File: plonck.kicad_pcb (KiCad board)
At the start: 2 copper layers, 228.6 x 76.2 mm, 127 parts, among them J1 Battery_connector, J2 SWD, Q1 Q_PMOS_DSG, U1 SRV05-4, U2 MCP73831-2-OT, U3 XC6206PxxxMR-Regulator_Linear, U4 nRF52840_holyiot_18010, q1 USB4085-GF-A_REVA

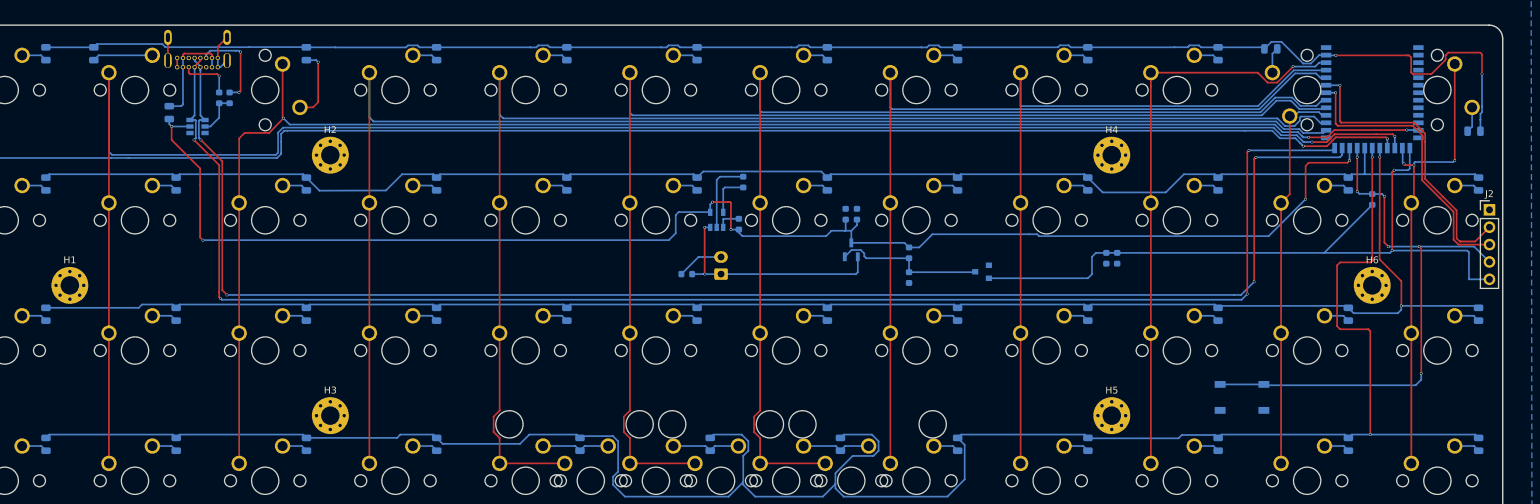
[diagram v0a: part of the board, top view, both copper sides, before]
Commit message: updated some fooprints and added lcsc part numbers
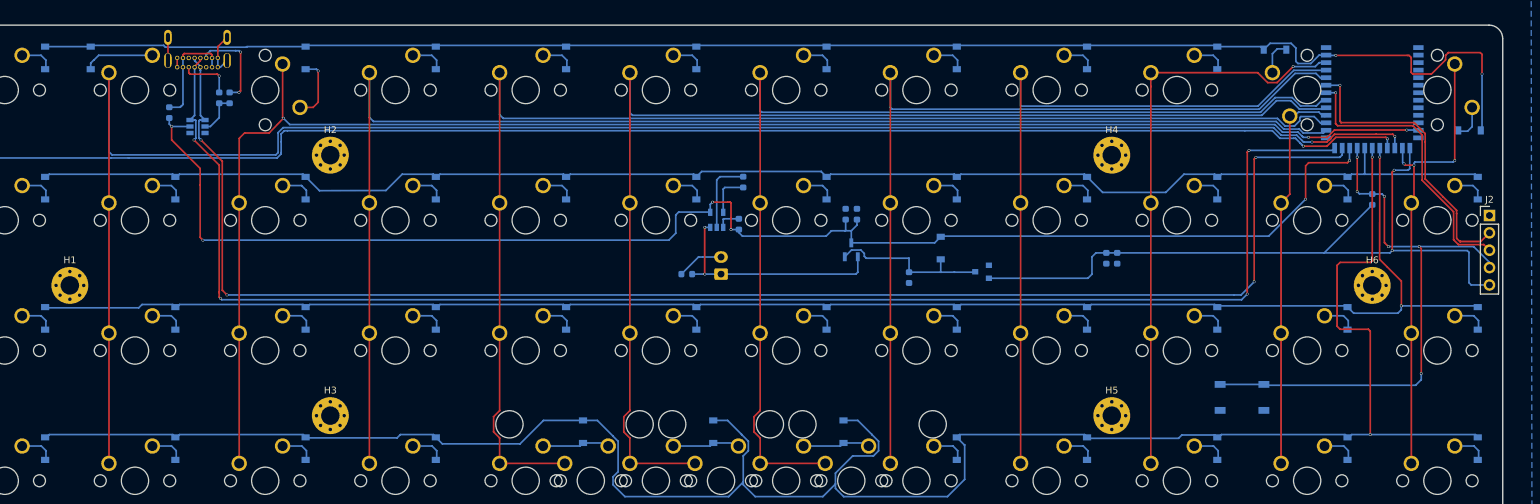
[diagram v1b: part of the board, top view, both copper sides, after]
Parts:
- C5: value 4,7uF -> 4.7uF
- D1, D10, D11, D12, D13, D14, D15, D16, D17, D18, D19, D2, D20, D21, D22, D23, D24, D25, D26, D27, D28, D29, D3, D30, D31, D32, D33, D34, D35, D36, D37, D38, D39, D4, D40, D41, D42, D43, D44, D45, D46, D47, D48, D5, D6, D7, D8, D9: footprint Diode_SMD:D_0805_2012Metric -> Diode_SMD:D_SOD-123
- D49: footprint Diode_SMD:D_0603_1608Metric -> Diode_SMD:D_SOD-123
- F1: footprint Fuse:Fuse_0805_2012Metric -> Fuse:Fuse_0603_1608Metric
- R1, R2: value 5.1k -> 5.1k Ω
- R5: value 100kΩ -> 100k Ω
- R6: value 10kΩ -> 10k Ω
- moved D49 4.69 mm to (178.2, 56.5)
- moved D41 1.89 mm to (125.9, 83.3)
- moved D42 1.89 mm to (144.9, 83.3)
- moved D43 1.89 mm to (164.0, 83.3)
- moved J2 0.83 mm to (258.4, 51.7)
- moved D2 0.76 mm to (53.8, 28.6)
- moved D12 0.67 mm to (255.5, 39.2)
- moved D44 0.65 mm to (180.5, 85.8)
- moved D45 0.65 mm to (199.6, 85.8)
- moved D47 0.65 mm to (237.7, 85.8)
- moved D48 0.65 mm to (256.7, 85.8)
- moved D37 0.65 mm to (47.2, 85.8)
- moved D38 0.65 mm to (66.2, 85.8)
- moved D39 0.65 mm to (85.3, 85.8)
- moved D40 0.65 mm to (104.3, 85.8)
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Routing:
- net Row4: track 314.8 -> 317.0 mm
- net Net-(C5-Pad1): track 22.3 -> 24.2 mm
- net Net-(D2-Pad2): track 8.85 -> 10.4 mm
- net Net-(D12-Pad2): track 3.75 -> 5.17 mm
- net Net-(D47-Pad2): track 3.78 -> 5.18 mm
- net Net-(D45-Pad2): track 3.78 -> 5.18 mm
- net Net-(D44-Pad2): track 3.78 -> 5.18 mm
- net Net-(D48-Pad2): track 3.78 -> 5.18 mm
- net Net-(D40-Pad2): track 3.78 -> 5.18 mm
- net Net-(D39-Pad2): track 3.78 -> 5.18 mm
- net Net-(D38-Pad2): track 3.78 -> 5.18 mm
- net Net-(D37-Pad2): track 3.78 -> 5.18 mm
- net Net-(D46-Pad2): track 3.78 -> 5.18 mm
- net Net-(D23-Pad2): track 3.77 -> 5.14 mm
- net Net-(D20-Pad2): track 3.77 -> 5.14 mm
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
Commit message: added ground fill on top layer
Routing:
- added copper zone on F.Cu, net (none)

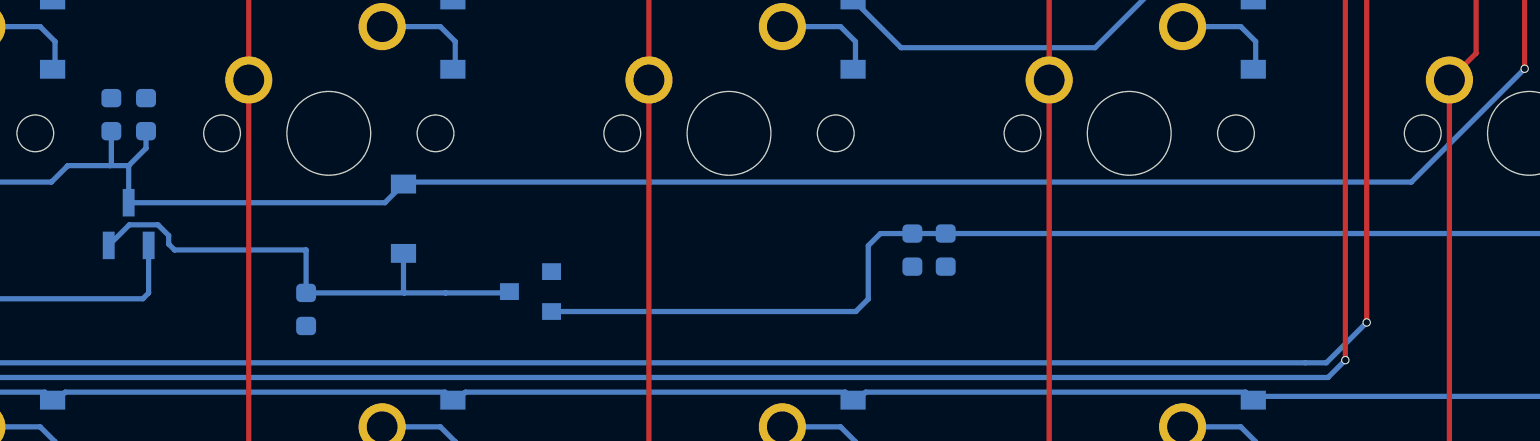
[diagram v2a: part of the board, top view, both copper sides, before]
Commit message: updated parts and fixed ground fill
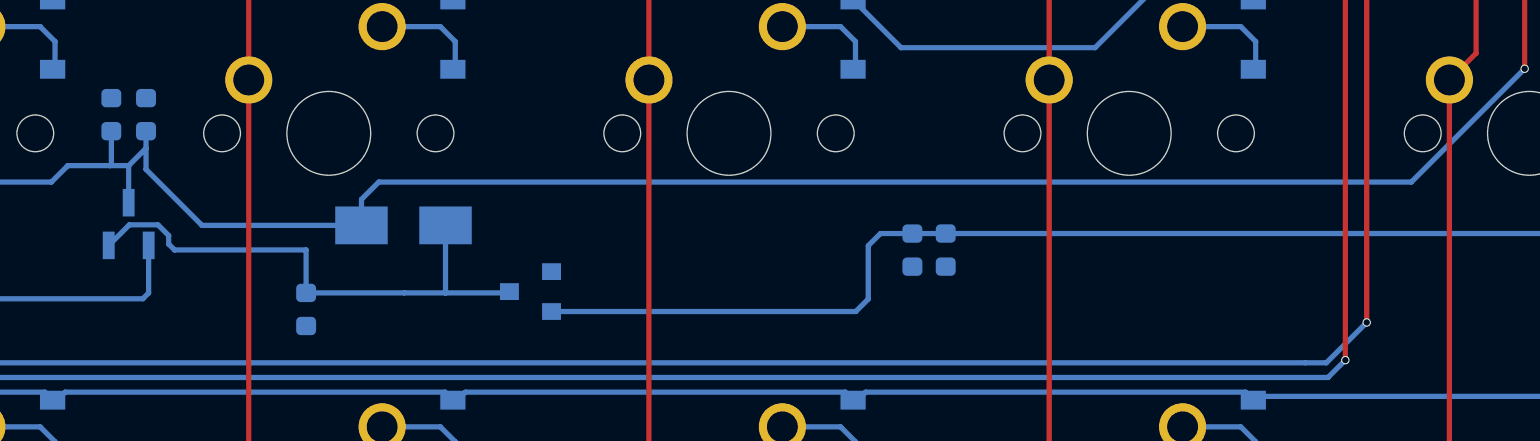
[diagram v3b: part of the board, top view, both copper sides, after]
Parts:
- D49: value B130-E3 -> B130LAW-7-F; footprint Diode_SMD:D_SOD-123 -> Diode_SMD:D_SMA
- moved D49 0.32 mm to (178.2, 56.8), turned to 180 degrees
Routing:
- net VBUS: track 214.7 -> 217.2 mm
- net Net-(C5-Pad1): track 24.2 -> 25.5 mm
- added copper zone on F.Cu, net GND
- removed copper zone on F.Cu, net (none)

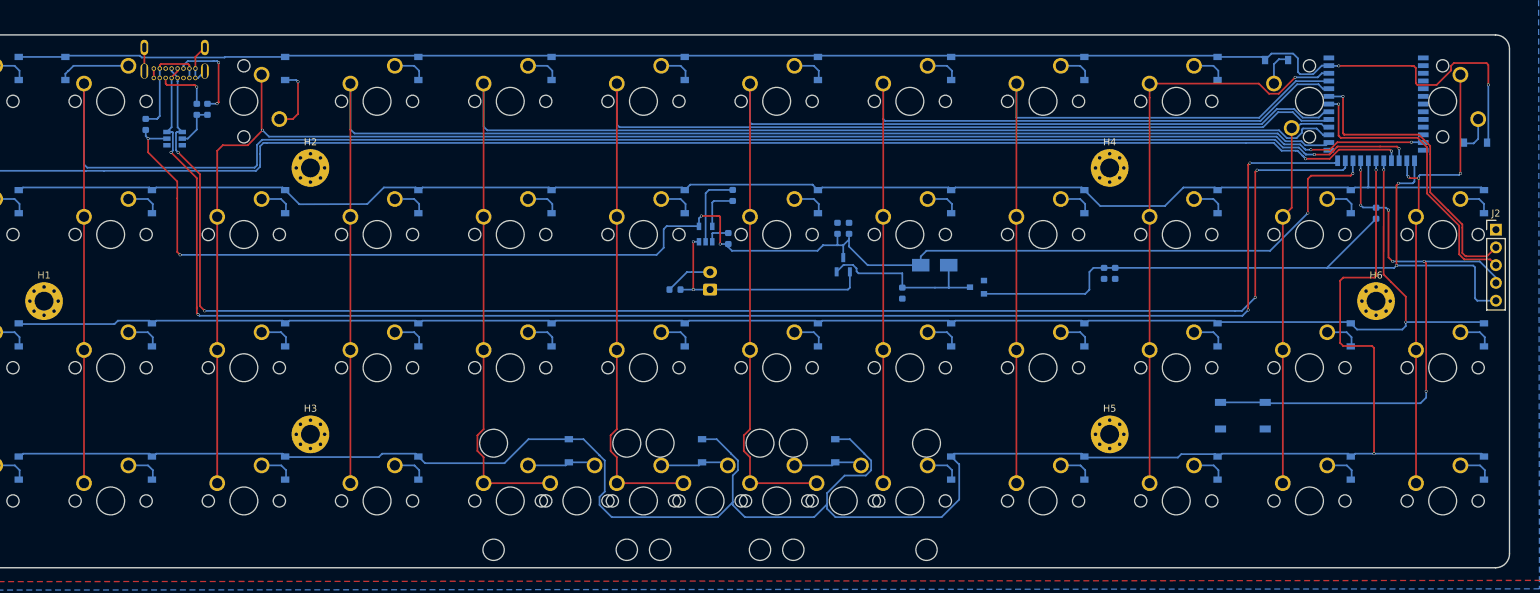
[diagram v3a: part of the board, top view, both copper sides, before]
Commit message: fixing up via sizes and ground planes
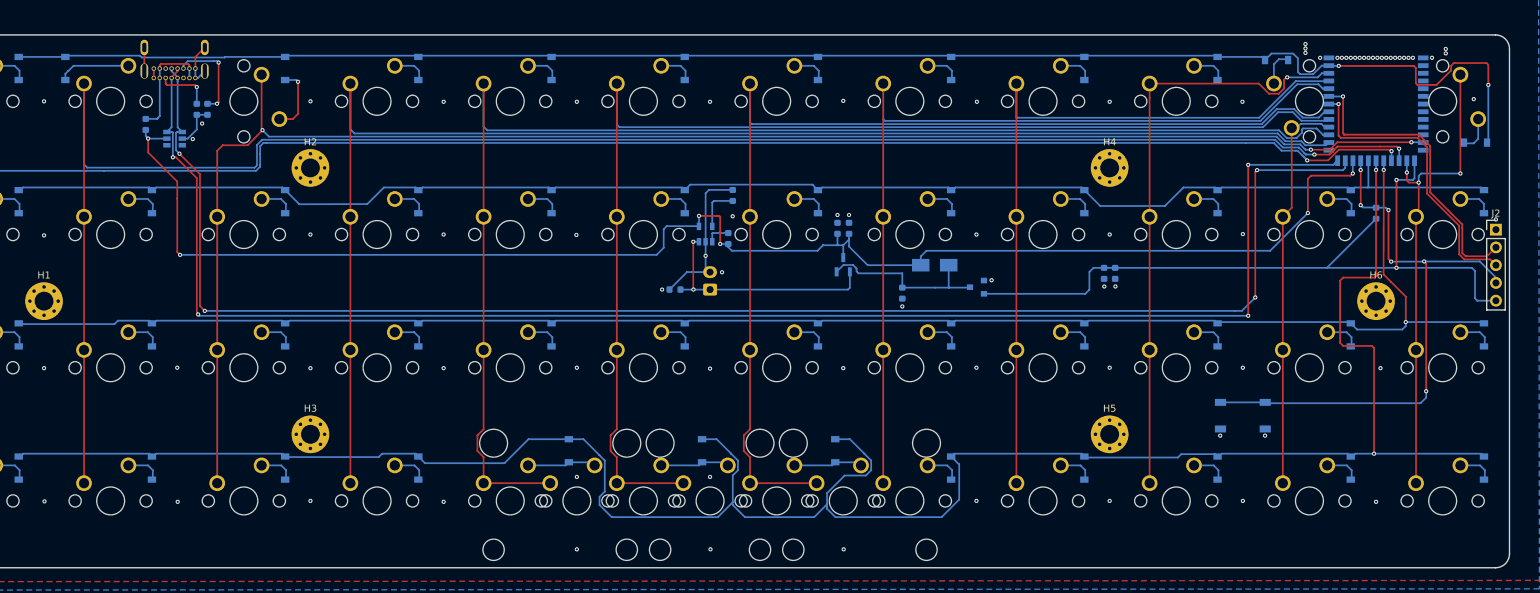
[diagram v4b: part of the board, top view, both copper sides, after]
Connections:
- H1 pad 1: (no net) -> GND
- H2 pad 1: (no net) -> GND
- H3 pad 1: (no net) -> GND
- H4 pad 1: (no net) -> GND
- H5 pad 1: (no net) -> GND
- H6 pad 1: (no net) -> GND
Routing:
- net GND: track 35.5 -> 40.1 mm, vias 0 -> 81
- net D+: track 222.8 -> 223.7 mm
- net Col12: track 68.3 -> 69.1 mm
- net Col10: track 84.6 -> 85.3 mm
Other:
- rule via_min_size: 0.4 -> 0.6

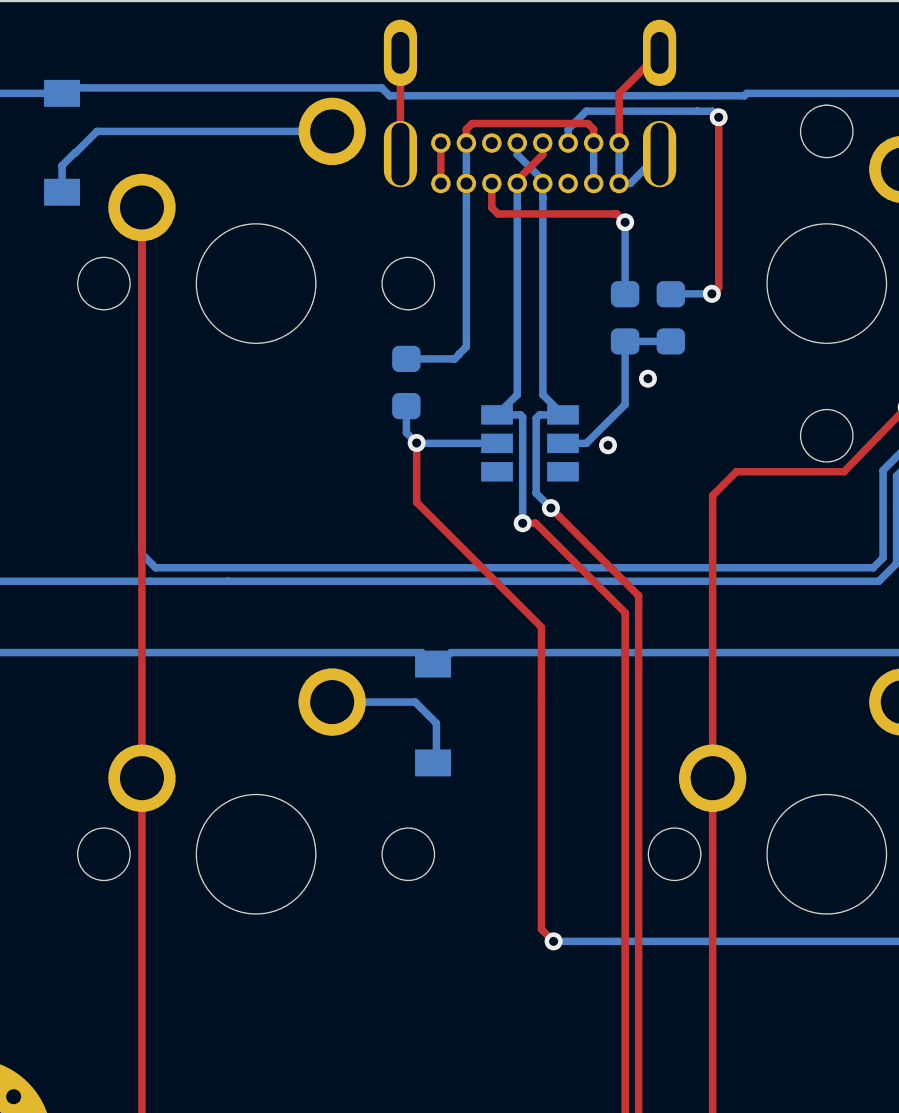
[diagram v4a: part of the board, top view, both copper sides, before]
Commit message: added missing lcsc part number
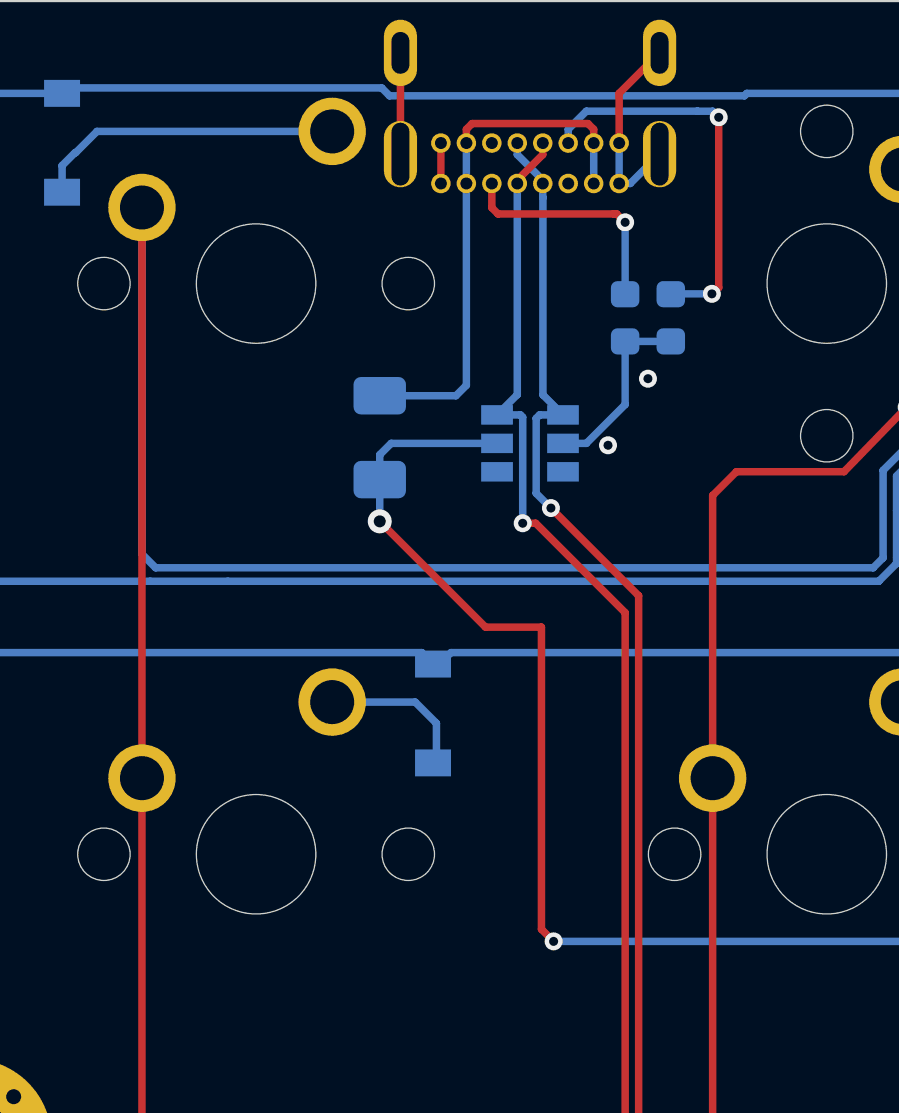
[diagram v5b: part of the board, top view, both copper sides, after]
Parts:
- C1, C2: value 47 uf -> 47uF
- F1: value 500mah -> SMD Fuse Fast Blow 500mA; footprint Fuse:Fuse_0603_1608Metric -> Fuse:Fuse_1206_3216Metric
- R1, R2: value 5.1k Ω -> 5.1k
- R3: value 470 Ω -> 470
- R4, R6: value 10k Ω -> 10k
- R5: value 100k Ω -> 100k
- moved F1 2.04 mm to (64.5, 38.5)
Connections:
- H1 pad 1: GND -> (no net)
- H2 pad 1: GND -> (no net)
- H3 pad 1: GND -> (no net)
- H4 pad 1: GND -> (no net)
- H5 pad 1: GND -> (no net)
- H6 pad 1: GND -> (no net)
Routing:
- net Net-(F1-Pad2): track 15.7 -> 17.8 mm
- net VBUS: track 217.4 -> 218.8 mm

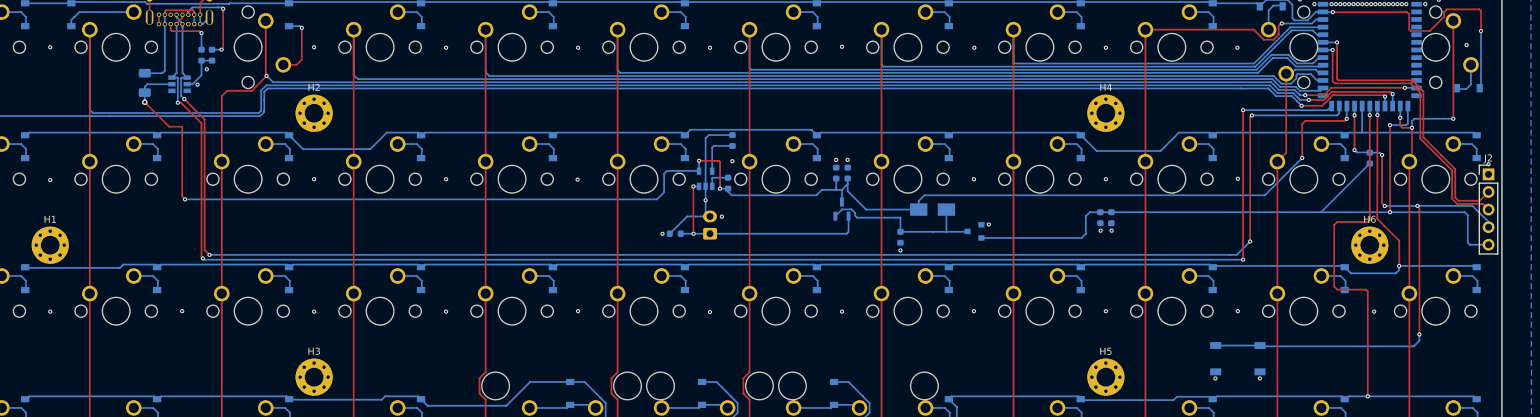
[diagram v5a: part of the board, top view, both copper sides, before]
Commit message: bunch of fixes and changes to use only basic parts from lcsc
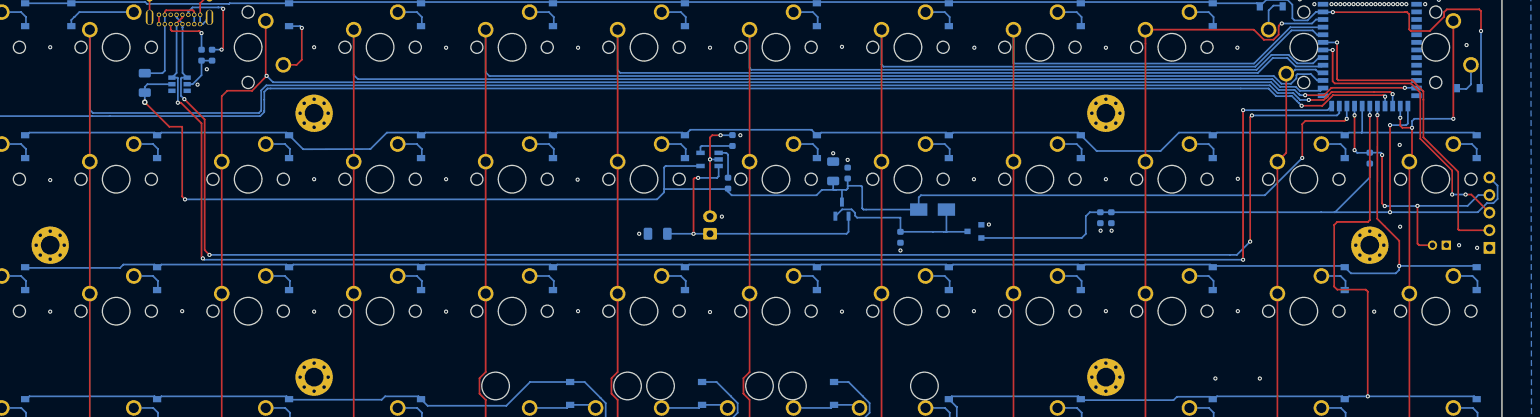
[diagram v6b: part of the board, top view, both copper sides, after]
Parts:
- removed S1: PTS525SM15SMTR2LFS, PTS525SM15SMTR2LFS:SW_PTS525SM15SMTR2LFS
- added J3: Reset, Connector_PinHeader_2.00mm:PinHeader_1x02_P2.00mm_Vertical, B.Cu at (252.3, 61.9)
- C1, C2: footprint Capacitor_SMD:C_0603_1608Metric -> Capacitor_SMD:C_1206_3216Metric
- D49: value B130LAW-7-F -> SS14
- H1, H2, H3, H4, H5, H6, J2: moved to B.Cu
- U2: value MCP73831-2-OT -> TP4054-42-SOT25-R; footprint Package_TO_SOT_SMD:SOT-23-5 -> Package_TO_SOT_SMD:TSOT-23-5
- moved J2 10.6 mm to (258.6, 62.3)
- moved U2 2.85 mm to (146.0, 49.5), turned to 180 degrees
- moved C2 2.54 mm to (138.5, 60.3)
- moved C1 0.51 mm to (163.8, 51.2)
- renumbered C4 to C3, C3 to C4
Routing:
- net RESET: track 84.3 -> 41.8 mm, vias 6 -> 5
- net +BATT: track 34.2 -> 41.7 mm
- net GND: track 40.1 -> 33.7 mm, vias 81 -> 85
- net SWDIO: track 43.3 -> 47.1 mm
- net VBUS: track 218.8 -> 220.9 mm, vias 6 -> 4
- net Net-(R3-Pad2): track 3.50 -> 4.80 mm
- net Net-(R4-Pad1): track 6.43 -> 5.52 mm
- net +3V3: track 108.2 -> 108.9 mm
- net SWCLK: track 42.4 -> 42.3 mm, vias 1 -> 3
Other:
- board text added: "Reset"
